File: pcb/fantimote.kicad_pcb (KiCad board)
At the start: 2 copper layers, 214 parts, among them IC701 ADXL345, J1001 ISP_tiny, J301 BAT+, J302 BAT-, J401 FTDI, J402 DIGITAL_DEBUG, J403 ANALOG_DEBUG, J404 ISP_atmega, J901 USB_OTG, M901 Vibration_motor, Q301 S8050, Q302 S8050, Q601 BC807, Q602 BC807, Q603 BC807, Q604 BC807, Q605 S8050, Q606 S8050, Q607 S8050, Q608 S8050, Q609 S8050, Q610 S8050, Q801 S8050, Q802 S8050, Q901 S8050, SW401 RESET, U1001 ATTINY85-20SU, U101 mounting_hole, U102 mounting_hole, U103 mounting_hole, U104 mounting_hole, U105 mounting_hole, U106 mounting_hole, U201 MC34063, U401 ATMEGA328-AU, U501 TPS4056, U601 74HC02, U602 74HC02, U603 74HC595, U801 TSDP341xx, Y401 Crystal

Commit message: routing
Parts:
- removed U102, U104, U106: mounting_hole, Mounting_Holes:MountingHole_3.2mm_M3_Pad_Via
- C1001, R1001, R1002, R1003, R1004, R1005, R1006, U1001: moved to B.Cu
- moved U101 221.4 mm to (47.6, 153.7)
- moved U105 209.9 mm to (66.7, 33.0)
- moved TP901 199.4 mm to (105.4, 176.5)
- moved TP502 198.9 mm to (112.4, 176.5)
- moved TP802 197.0 mm to (105.4, 185.4)
- moved TP503 195.5 mm to (112.4, 185.4)
- moved U103 193.4 mm to (88.9, 185.4)
- moved TP202 181.1 mm to (108.6, 158.8)
- moved TP201 175.2 mm to (112.4, 168.9)
- moved C1001 172.3 mm to (70.5, 64.8), turned to 270 degrees
- moved TP501 169.0 mm to (105.4, 168.9)
- moved U1001 167.6 mm to (66.7, 64.1), turned to 90 degrees
- moved TP701 165.3 mm to (105.4, 150.5)
- moved R1003 163.6 mm to (75.6, 59.1), turned to 180 degrees
- moved TP801 162.0 mm to (105.4, 22.2)
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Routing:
- net A7: track 0.00 -> 67.8 mm, vias 0 -> 2
- net A6: track 0.00 -> 66.8 mm, vias 0 -> 1
- net MOSI: track 0.00 -> 54.5 mm
- net MISO: track 0.00 -> 46.8 mm
- net RESET: track 0.00 -> 46.5 mm
- net Net-(D601-Pad2): track 0.00 -> 44.0 mm
- net A3: track 0.00 -> 41.2 mm
- net TXD: track 0.00 -> 37.4 mm
- net RXI: track 0.00 -> 31.4 mm
- net SCK: track 0.00 -> 30.4 mm
- net Net-(Q608-Pad2): track 0.00 -> 26.7 mm
- net A5: track 0.00 -> 24.8 mm
- net A4: track 0.00 -> 24.3 mm
- net Net-(Q607-Pad2): track 0.00 -> 23.5 mm
- net CH_UP: track 0.00 -> 22.0 mm
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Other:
- board outline added: 79.4 x 174.6 mm

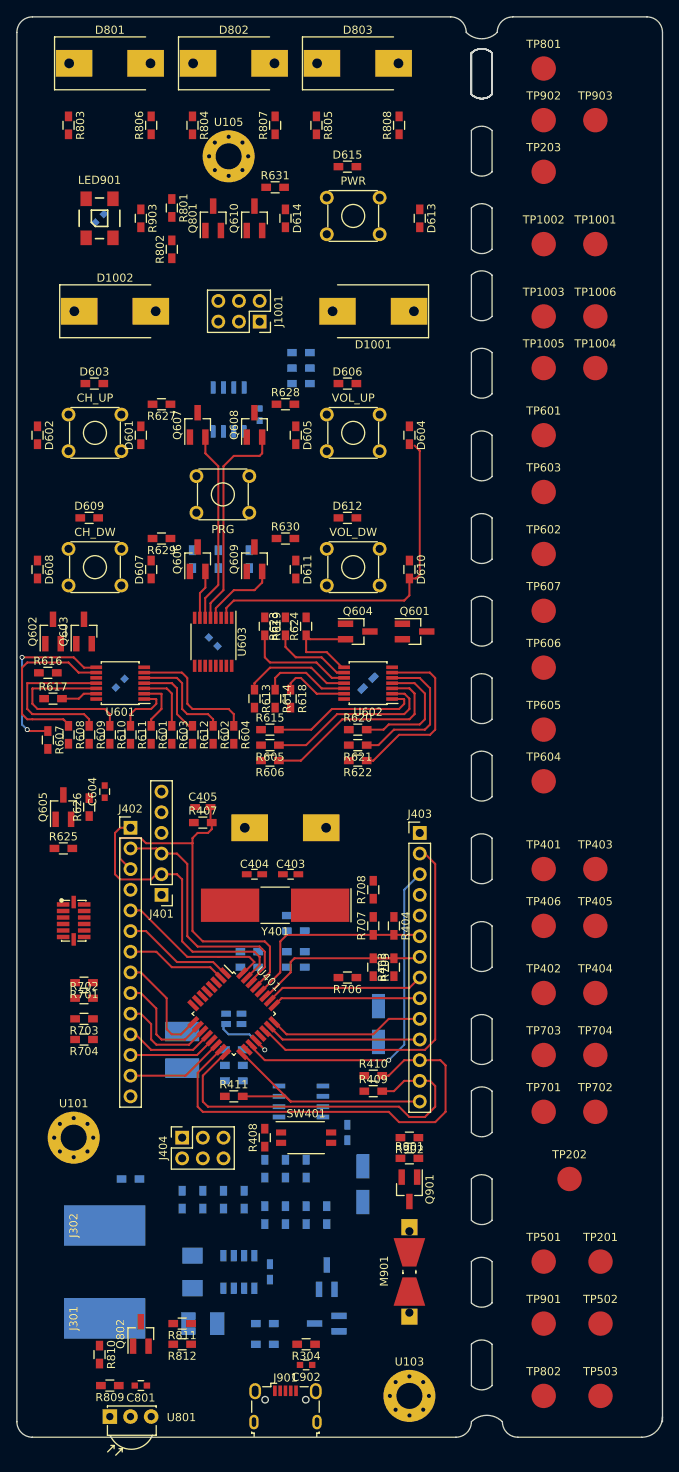
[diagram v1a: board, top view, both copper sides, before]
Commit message: new routes, changed few parts for shorter tracks
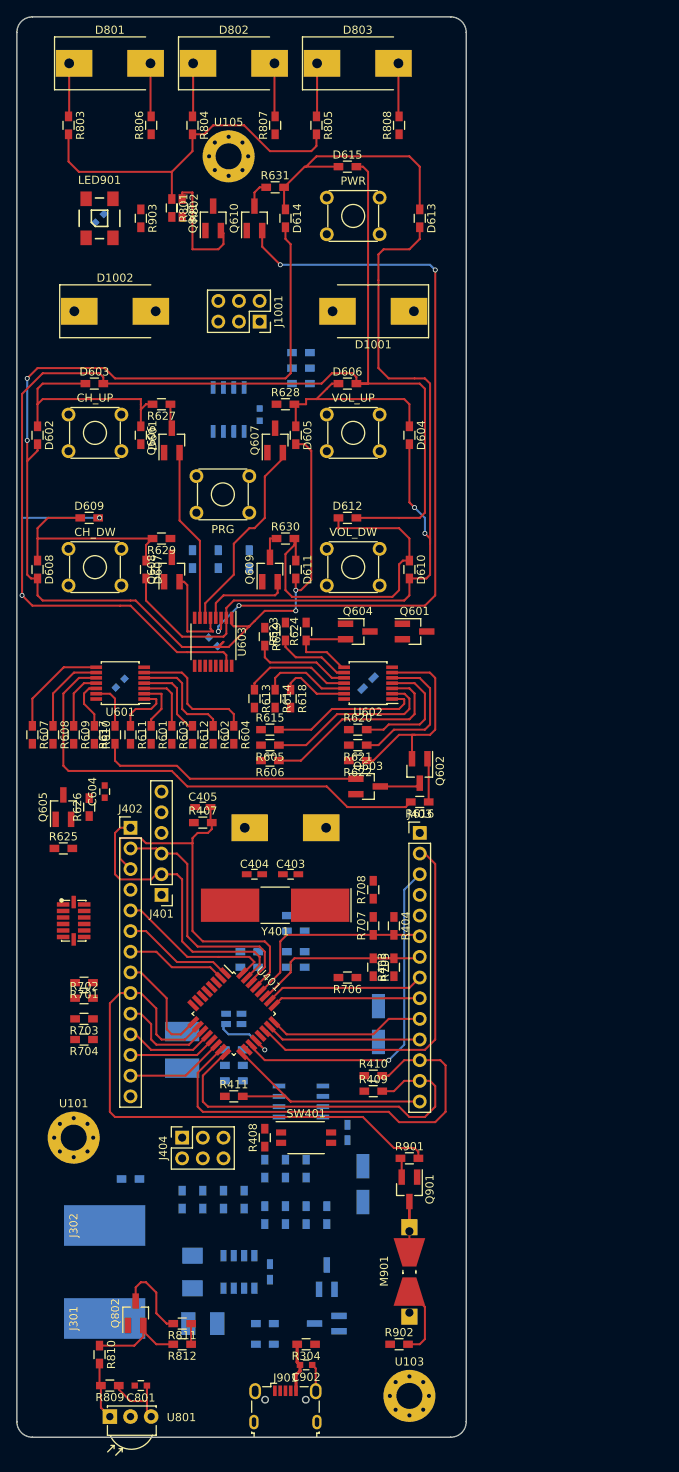
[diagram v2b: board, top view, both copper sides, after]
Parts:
- removed TP1001: USB_D-, Measurement_Points:Measurement_Point_Round-SMD-Pad_Big
- removed TP1002: USB_D+, Measurement_Points:Measurement_Point_Round-SMD-Pad_Big
- removed TP1003: tiny_RESET, Measurement_Points:Measurement_Point_Round-SMD-Pad_Big
- removed TP1004: RXD, Measurement_Points:Measurement_Point_Round-SMD-Pad_Big
- removed TP1005: TXI, Measurement_Points:Measurement_Point_Round-SMD-Pad_Big
- removed TP1006: DTR, Measurement_Points:Measurement_Point_Round-SMD-Pad_Big
- removed TP201: TEST_VBAT_DCDC, Measurement_Points:Measurement_Point_Round-SMD-Pad_Big
- removed TP202: TEST_GND_DCDC, Measurement_Points:Measurement_Point_Round-SMD-Pad_Big
- removed TP203: TEST_5V_DCDC, Measurement_Points:Measurement_Point_Round-SMD-Pad_Big
- removed TP401: PB6, Measurement_Points:Measurement_Point_Round-SMD-Pad_Big
- removed TP402: VBat, Measurement_Points:Measurement_Point_Round-SMD-Pad_Big
- removed TP403: PB7, Measurement_Points:Measurement_Point_Round-SMD-Pad_Big
- removed TP404: VPlus, Measurement_Points:Measurement_Point_Round-SMD-Pad_Big
- removed TP405: SDA, Measurement_Points:Measurement_Point_Round-SMD-Pad_Big
- removed TP406: SCL, Measurement_Points:Measurement_Point_Round-SMD-Pad_Big
- removed TP501: temp, Measurement_Points:Measurement_Point_Round-SMD-Pad_Big
- removed TP502: Charge, Measurement_Points:Measurement_Point_Round-SMD-Pad_Big
- removed TP503: Standby, Measurement_Points:Measurement_Point_Round-SMD-Pad_Big
- removed TP601: PWR_or_VOL_UP, Measurement_Points:Measurement_Point_Round-SMD-Pad_Big
- removed TP602: VOL_DW_or_CH_UP, Measurement_Points:Measurement_Point_Round-SMD-Pad_Big
- removed TP603: CH_DW_or_PRG, Measurement_Points:Measurement_Point_Round-SMD-Pad_Big
- removed TP604: GATE12, Measurement_Points:Measurement_Point_Round-SMD-Pad_Big
- removed TP605: ring_led_data, Measurement_Points:Measurement_Point_Round-SMD-Pad_Big
- removed TP606: ring_led_clock, Measurement_Points:Measurement_Point_Round-SMD-Pad_Big
- removed TP607: ring_led_clock2, Measurement_Points:Measurement_Point_Round-SMD-Pad_Big
- removed TP701: adxl_int1, Measurement_Points:Measurement_Point_Round-SMD-Pad_Big
- removed TP702: adxl_int2, Measurement_Points:Measurement_Point_Round-SMD-Pad_Big
- removed TP703: ADXL_CLK, Measurement_Points:Measurement_Point_Round-SMD-Pad_Big
- removed TP704: ADXL_DATA, Measurement_Points:Measurement_Point_Round-SMD-Pad_Big
- removed TP801: IR_SEND, Measurement_Points:Measurement_Point_Round-SMD-Pad_Big
- removed TP802: IR_Received, Measurement_Points:Measurement_Point_Round-SMD-Pad_Big
- removed TP901: motor, Measurement_Points:Measurement_Point_Round-SMD-Pad_Big
- removed TP902: WS2812, Measurement_Points:Measurement_Point_Round-SMD-Pad_Big
- removed TP903: DOUT_WS2812, Measurement_Points:Measurement_Point_Round-SMD-Pad_Big
- moved R616 48.4 mm to (90.2, 112.4), turned to 180 degrees
- moved Q602 48.2 mm to (90.2, 108.6), turned to 270 degrees
- moved Q603 39.8 mm to (83.8, 110.5), turned to 0 degrees
- moved R902 25.4 mm to (87.6, 179.1), turned to 0 degrees
- moved Q608 20.5 mm to (59.7, 83.8)
- moved Q606 14.9 mm to (59.7, 67.9)
- moved Q607 9.71 mm to (72.4, 67.9)
- moved R617 8.82 mm to (52.7, 104.1), turned to 90 degrees
- moved R802 5.24 mm to (61.0, 39.4), turned to 270 degrees
- moved Q802 2.62 mm to (55.2, 175.3)
- moved Q609 2.29 mm to (71.8, 83.8)
- moved R607 2.01 mm to (42.5, 104.1)
- moved R608 1.91 mm to (45.1, 104.1)
- moved R609 1.91 mm to (47.6, 104.1)
- moved R610 1.91 mm to (50.2, 104.1)
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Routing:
- net Net-(D603-Pad2): track 0.00 -> 179.9 mm, vias 0 -> 2
- net Net-(D602-Pad2): track 0.00 -> 147.8 mm, vias 0 -> 4
- net Net-(Q610-Pad2): track 0.00 -> 95.2 mm, vias 0 -> 4
- net Net-(D601-Pad2): track 44.0 -> 110.9 mm, vias 0 -> 2
- net Net-(R616-Pad2): track 0.00 -> 58.8 mm
- net D6: track 13.2 -> 70.3 mm
- net Net-(Q801-Pad3): track 0.00 -> 44.3 mm
- net Net-(D610-Pad1): track 0.00 -> 42.4 mm
- net Net-(Q603-Pad1): track 0.00 -> 32.6 mm
- net Net-(D613-Pad1): track 0.00 -> 30.8 mm
- net Net-(D601-Pad1): track 0.00 -> 28.8 mm
- net Net-(D607-Pad1): track 0.00 -> 26.9 mm
- net Net-(D604-Pad1): track 0.00 -> 24.0 mm
- net Net-(Q606-Pad2): track 5.99 -> 21.4 mm
- net PRG: track 21.2 -> 6.26 mm
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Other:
- board size 79.4 x 174.6 mm -> 55.2 x 174.6 mm
- net class GNDD added: clearance 0.2, trace_width 0.4, via_dia 0.6, via_drill 0.4

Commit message: WIP: large amount of new routes, removed testpoints
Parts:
- removed J401: FTDI, Socket_Strips:Socket_Strip_Straight_1x06_Pitch2.54mm
- D1001, D1002: footprint Diodes_SMD:D_SMC-RM10_Universal_Handsoldering -> Diodes_SMD:D_SMB-SMC_Universal_Handsoldering; moved to B.Cu
- D201: footprint Diodes_SMD:D_SMC-RM10_Universal_Handsoldering -> Diodes_SMD:D_SMB-SMC_Universal_Handsoldering
- R304: moved to B.Cu
- moved D201 44.2 mm to (85.7, 158.1), turned to 0 degrees
- moved C202 37.5 mm to (50.8, 154.9), turned to 180 degrees
- moved D1001 31.9 mm to (52.7, 54.6)
- moved R702 31.0 mm to (69.8, 113.7), turned to 180 degrees
- moved IC701 30.8 mm to (76.2, 115.6), turned to 270 degrees
- moved R701 30.5 mm to (69.8, 112.4), turned to 0 degrees
- moved C403 30.5 mm to (45.1, 130.2), turned to 90 degrees
- moved R704 28.9 mm to (67.3, 119.4), turned to 0 degrees
- moved C404 28.4 mm to (45.1, 135.3), turned to 270 degrees
- moved R703 28.4 mm to (67.3, 117.5), turned to 0 degrees
- moved R304 25.7 mm to (52.1, 170.2), turned to 270 degrees
- moved Y401 25.3 mm to (48.3, 132.7), turned to 270 degrees
- moved C201 25.0 mm to (60.3, 169.5)
- moved L201 24.8 mm to (85.1, 148.6), turned to 90 degrees
- moved R1002 16.2 mm to (59.7, 60.3), turned to 90 degrees
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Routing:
- net +5V: track 13.6 -> 609.3 mm, vias 0 -> 26
- net GNDD: track 6.07 -> 224.5 mm, vias 0 -> 7
- net USB_D+: track 0.00 -> 203.3 mm, vias 0 -> 5
- net USB_D-: track 0.00 -> 201.8 mm, vias 0 -> 5
- net CH_UP: track 10.5 -> 171.9 mm, vias 0 -> 10
- net D5: track 13.7 -> 147.9 mm, vias 0 -> 4
- net A3: track 41.2 -> 175.3 mm, vias 0 -> 1
- net D10: track 12.1 -> 131.7 mm, vias 0 -> 4
- net CH_DW: track 7.27 -> 122.5 mm, vias 0 -> 4
- net +BATT: track 0.00 -> 110.9 mm, vias 0 -> 6
- net -BATT: track 0.00 -> 101.2 mm
- net RESET: track 46.5 -> 142.6 mm, vias 0 -> 4
- net PRG: track 6.26 -> 102.2 mm, vias 0 -> 5
- net A6: track 66.8 -> 157.7 mm, vias 1 -> 4
- net A7: track 59.4 -> 147.4 mm, vias 0 -> 5
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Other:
- net class +5V added: clearance 0.2, trace_width 0.35, via_dia 0.6, via_drill 0.4

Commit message: added 3d files, added routes, added copper layers, added silkscreen
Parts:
- added G***: LOGO, fanti:fanti_inverse, F.Cu at (85.1, 54.0)
- U1001: value ATTINY85-20SU -> ATTINY85
- moved R1002 0.64 mm to (60.3, 60.3)
- moved R1003 0.63 mm to (62.2, 60.3)
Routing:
- net GND: track 0.00 -> 115.4 mm, vias 0 -> 24
- net (no net): track 0.00 -> 43.2 mm, vias 0 -> 23
- net +5V: track 609.3 -> 642.6 mm
- net D5: track 147.9 -> 128.2 mm
- net Net-(D603-Pad2): track 183.2 -> 166.8 mm, vias 2 -> 3
- net Net-(L201-Pad2): track 46.1 -> 54.6 mm, vias 2 -> 0
- net RESET: track 142.6 -> 150.5 mm
- net CH_DW: track 122.5 -> 114.9 mm
- net CH_UP: track 171.9 -> 164.7 mm, vias 10 -> 11
- net A6: track 157.7 -> 154.4 mm
- net A4: track 24.3 -> 21.0 mm
- net Net-(R1002-Pad1): track 9.90 -> 12.4 mm
- net A5: track 24.8 -> 22.5 mm
- net PRG: track 102.2 -> 104.5 mm
- net A3: track 175.3 -> 177.5 mm
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- added copper zone on B.Cu, net GND
- added copper zone on F.Cu, net GND
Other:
- board text added: "BLACK"
- board text added: "RED"
- board text added: "fantimote v1 DEBUG"
- board text added: "marc 08/18"
